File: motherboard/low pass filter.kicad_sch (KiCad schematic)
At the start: 12 parts, among them U4 LM324

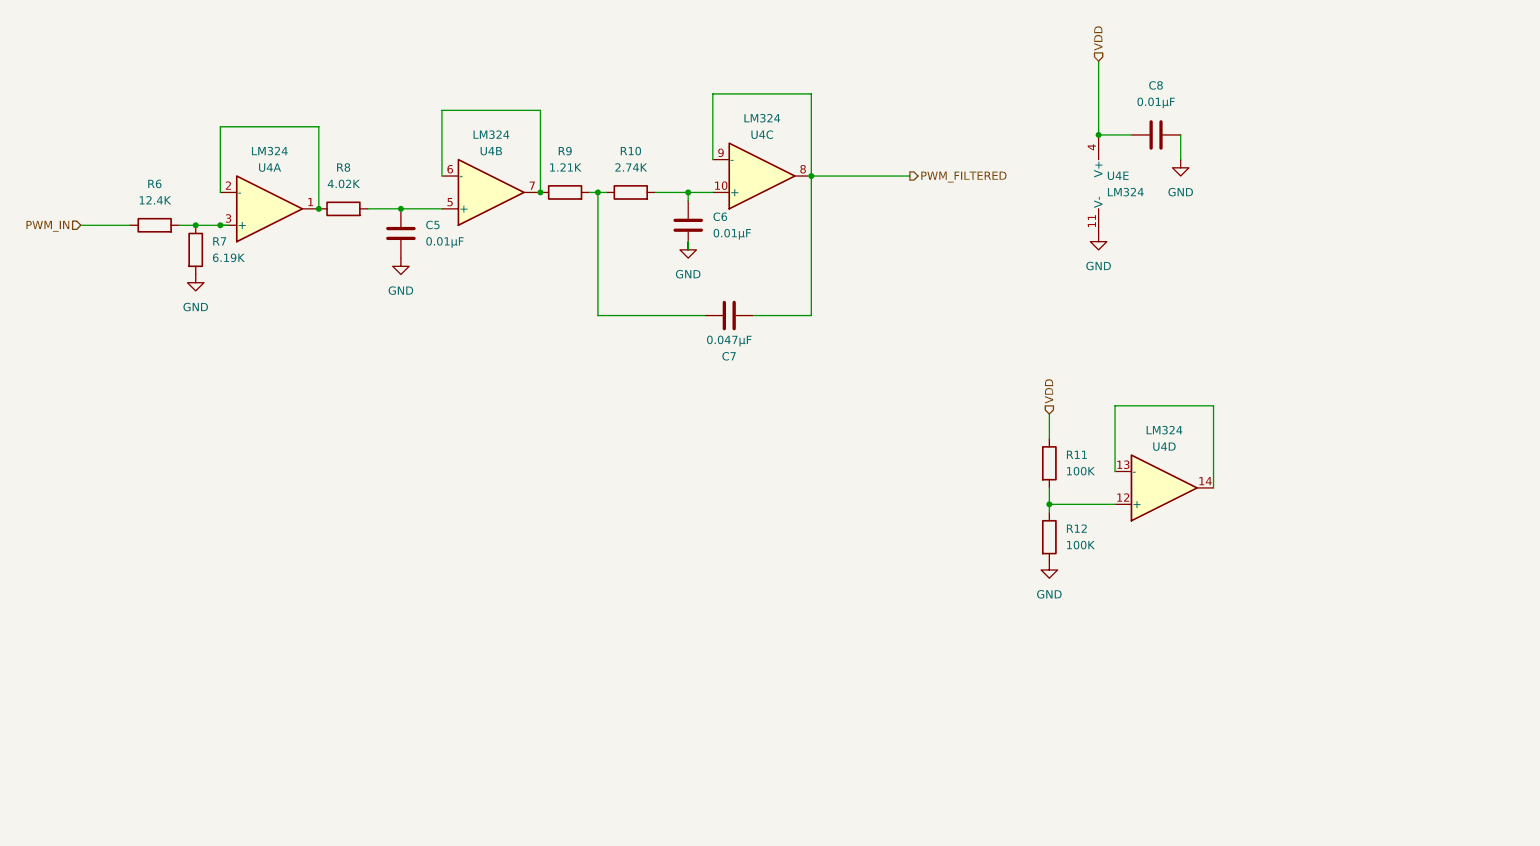
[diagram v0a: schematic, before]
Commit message: motherboard add test points
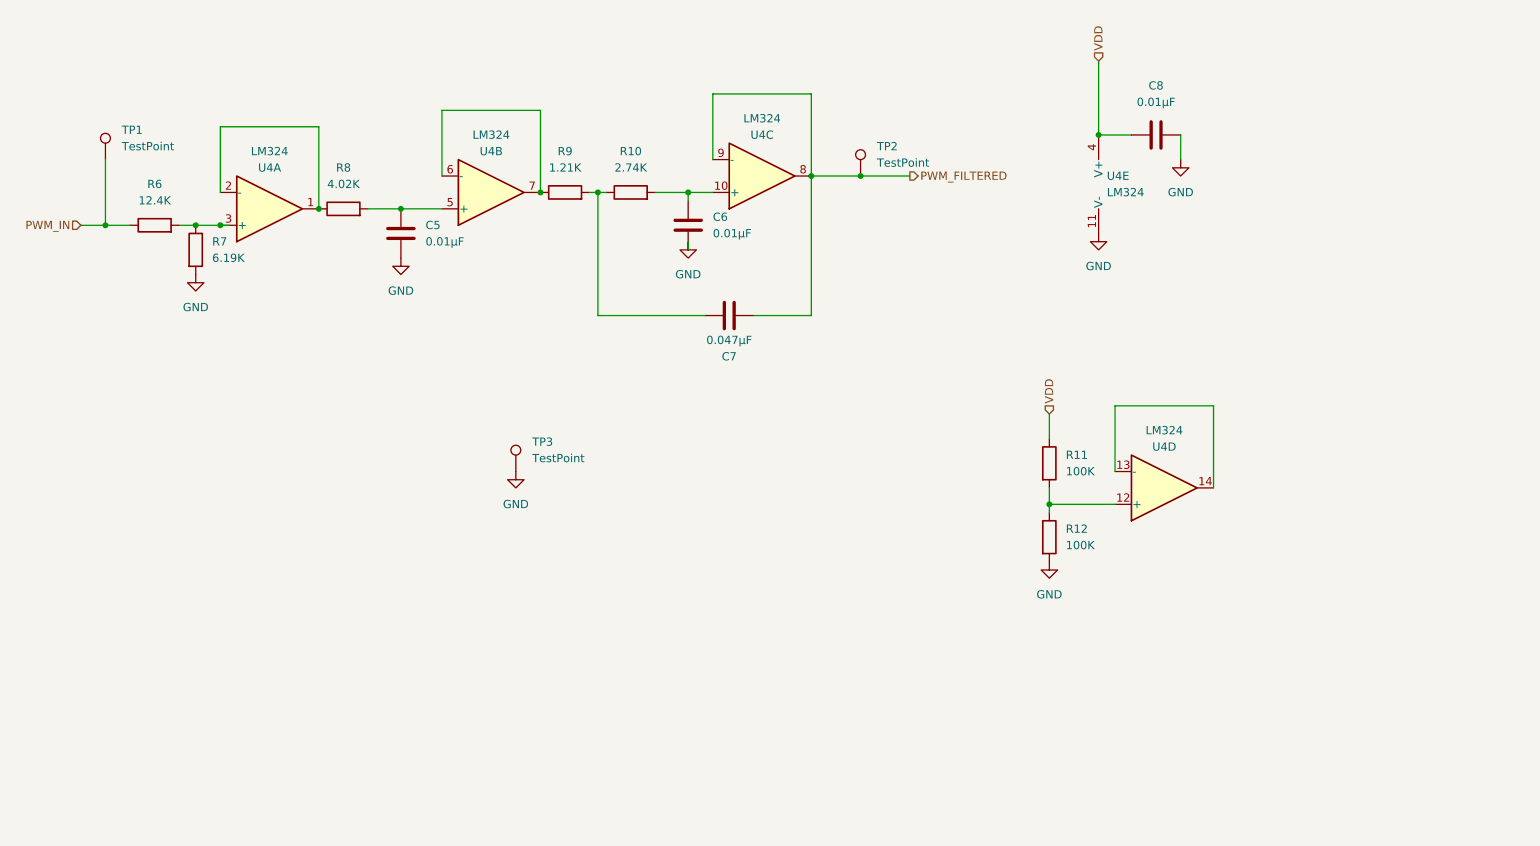
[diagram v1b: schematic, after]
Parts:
- added TP1, TP2: TestPoint, TestPoint:TestPoint_THTPad_D1.0mm_Drill0.5mm, symbol Connector:TestPoint
- added TP3: TestPoint, TestPoint:TestPoint_THTPad_1.0x1.0mm_Drill0.5mm, symbol Connector:TestPoint
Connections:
- net GND: now also TP3.1
- net PWM_FILTERED: now also TP2.1
- net PWM_IN: now also TP1.1
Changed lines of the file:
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@@
   (junction (at 97.79 53.34) (diameter 0) (color 0 0 0 0)
   )
+  (junction (at 147.32 50.8) (diameter 0) (color 0 0 0 0)
+  )
   (junction (at 63.5 55.88) (diameter 0) (color 0 0 0 0)
   )
@@
   (junction (at 76.2 55.88) (diameter 0) (color 0 0 0 0)
   )
+  (junction (at 30.48 58.42) (diameter 0) (color 0 0 0 0)
+  )
   (junction (at 106.68 53.34) (diameter 0) (color 0 0 0 0)
   )
@@
     (stroke (width 0) (type default))
   )
-  (wire (pts (xy 26.67 58.42) (xy 34.29 58.42))
+  (wire (pts (xy 26.67 58.42) (xy 30.48 58.42))
     (stroke (width 0) (type default))
   )
@@
     (stroke (width 0) (type default))
   )
+  (wire (pts (xy 30.48 58.42) (xy 34.29 58.42))
+    (stroke (width 0) (type default))
+  )
   (wire (pts (xy 201.93 86.36) (xy 186.69 86.36))
     (stroke (width 0) (type default))
@@
     (stroke (width 0) (type default))
   )
+  (wire (pts (xy 30.48 48.26) (xy 30.48 58.42))
+    (stroke (width 0) (type default))
+  )
   (wire (pts (xy 48.26 53.34) (xy 48.26 43.18))
     (stroke (width 0) (type default))
@@
     (stroke (width 0) (type default))
   )
+  (wire (pts (xy 147.32 50.8) (xy 154.94 50.8))
+    (stroke (width 0) (type default))
+  )
   (wire (pts (xy 176.53 101.6) (xy 176.53 102.87))
     (stroke (width 0) (type default))
@@
     (stroke (width 0) (type default))
   )
-  (wire (pts (xy 139.7 50.8) (xy 154.94 50.8))
+  (wire (pts (xy 139.7 50.8) (xy 147.32 50.8))
     (stroke (width 0) (type default))
   )
@@
         (path "/e63e39d7-6ac0-4ffd-8aa3-1841a4541b55/ea3171e1-d7f3-4749-80f8-d8022d132810"
           (reference "#PWR027") (unit 1)
+        )
+      )
+    )
+  )
+  (symbol (lib_id "power:GND") (at 93.98 96.52 0) (unit 1)
+    (in_bom yes) (on_board yes) (dnp no) (fields_autoplaced)
+    (property "Reference" "#PWR034" (at 93.98 102.87 0)
+      (effects (font (size 1.27 1.27)) hide)
+    )
+    (property "Value" "GND" (at 93.98 101.6 0)
+      (effects (font (size 1.27 1.27)))
+    )
+    (property "Footprint" "" (at 93.98 96.52 0)
+      (effects (font (size 1.27 1.27)) hide)
+    )
+    (property "Datasheet" "" (at 93.98 96.52 0)
+      (effects (font (size 1.27 1.27)) hide)
+    )
+    (pin "1")
+    (instances
+      (project "motherboard"
+        (path "/e63e39d7-6ac0-4ffd-8aa3-1841a4541b55/ea3171e1-d7f3-4749-80f8-d8022d132810"
+          (reference "#PWR034") (unit 1)
         )
       )
@@
     )
   )
+  (symbol (lib_id "Connector:TestPoint") (at 30.48 48.26 0) (unit 1)
+    (in_bom yes) (on_board yes) (dnp no) (fields_autoplaced)
+    (property "Reference" "TP1" (at 33.02 43.688 0)
+      (effects (font (size 1.27 1.27)) (justify left))
+    )
+    (property "Value" "TestPoint" (at 33.02 46.228 0)
+      (effects (font (size 1.27 1.27)) (justify left))
+    )
+    (property "Footprint" "TestPoint:TestPoint_THTPad_D1.0mm_Drill0.5mm" (at 35.56 48.26 0)
+      (effects (font (size 1.27 1.27)) hide)
+    )
+    (property "Datasheet" "~" (at 35.56 48.26 0)
+      (effects (font (size 1.27 1.27)) hide)
+    )
+    (pin "1")
+    (instances
+      (project "motherboard"
+        (path "/e63e39d7-6ac0-4ffd-8aa3-1841a4541b55/ea3171e1-d7f3-4749-80f8-d8022d132810"
+          (reference "TP1") (unit 1)
+        )
+      )
+    )
+  )
   (symbol (lib_id "Amplifier_Operational:LM324") (at 186.69 52.07 0) (unit 5)
     (in_bom yes) (on_board yes) (dnp no) (fields_autoplaced)
@@
     )
   )
+  (symbol (lib_id "Connector:TestPoint") (at 93.98 96.52 0) (unit 1)
+    (in_bom yes) (on_board yes) (dnp no) (fields_autoplaced)
+    (property "Reference" "TP3" (at 96.52 91.948 0)
+      (effects (font (size 1.27 1.27)) (justify left))
+    )
+    (property "Value" "TestPoint" (at 96.52 94.488 0)
+      (effects (font (size 1.27 1.27)) (justify left))
+    )
+    (property "Footprint" "TestPoint:TestPoint_THTPad_1.0x1.0mm_Drill0.5mm" (at 99.06 96.52 0)
+      (effects (font (size 1.27 1.27)) hide)
+    )
+    (property "Datasheet" "~" (at 99.06 96.52 0)
+      (effects (font (size 1.27 1.27)) hide)
+    )
+    (pin "1")
+    (instances
+      (project "motherboard"
+        (path "/e63e39d7-6ac0-4ffd-8aa3-1841a4541b55/ea3171e1-d7f3-4749-80f8-d8022d132810"
+          (reference "TP3") (unit 1)
+        )
+      )
+    )
+  )
   (symbol (lib_id "Amplifier_Operational:LM324") (at 90.17 53.34 0) (mirror x) (unit 2)
     (in_bom yes) (on_board yes) (dnp no)
@@
         )
       )
+    )
+  )
+  (symbol (lib_id "Connector:TestPoint") (at 147.32 50.8 0) (unit 1)
+    (in_bom yes) (on_board yes) (dnp no) (fields_autoplaced)
+    (property "Reference" "TP2" (at 149.86 46.228 0)
+      (effects (font (size 1.27 1.27)) (justify left))
+    )
+    (property "Value" "TestPoint" (at 149.86 48.768 0)
+      (effects (font (size 1.27 1.27)) (justify left))
+    )
+    (property "Footprint" "TestPoint:TestPoint_THTPad_D1.0mm_Drill0.5mm" (at 152.4 50.8 0)
+      (effects (font (size 1.27 1.27)) hide)
+    )
+    (property "Datasheet" "~" (at 152.4 50.8 0)
+      (effects (font (size 1.27 1.27)) hide)
+    )
+    (pin "1")
+    (instances
+      (project "motherboard"
+        (path "/e63e39d7-6ac0-4ffd-8aa3-1841a4541b55/ea3171e1-d7f3-4749-80f8-d8022d132810"
+          (reference "TP2") (unit 1)
+        )
+      )

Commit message: add 1st order low pass filter, with solder jumper
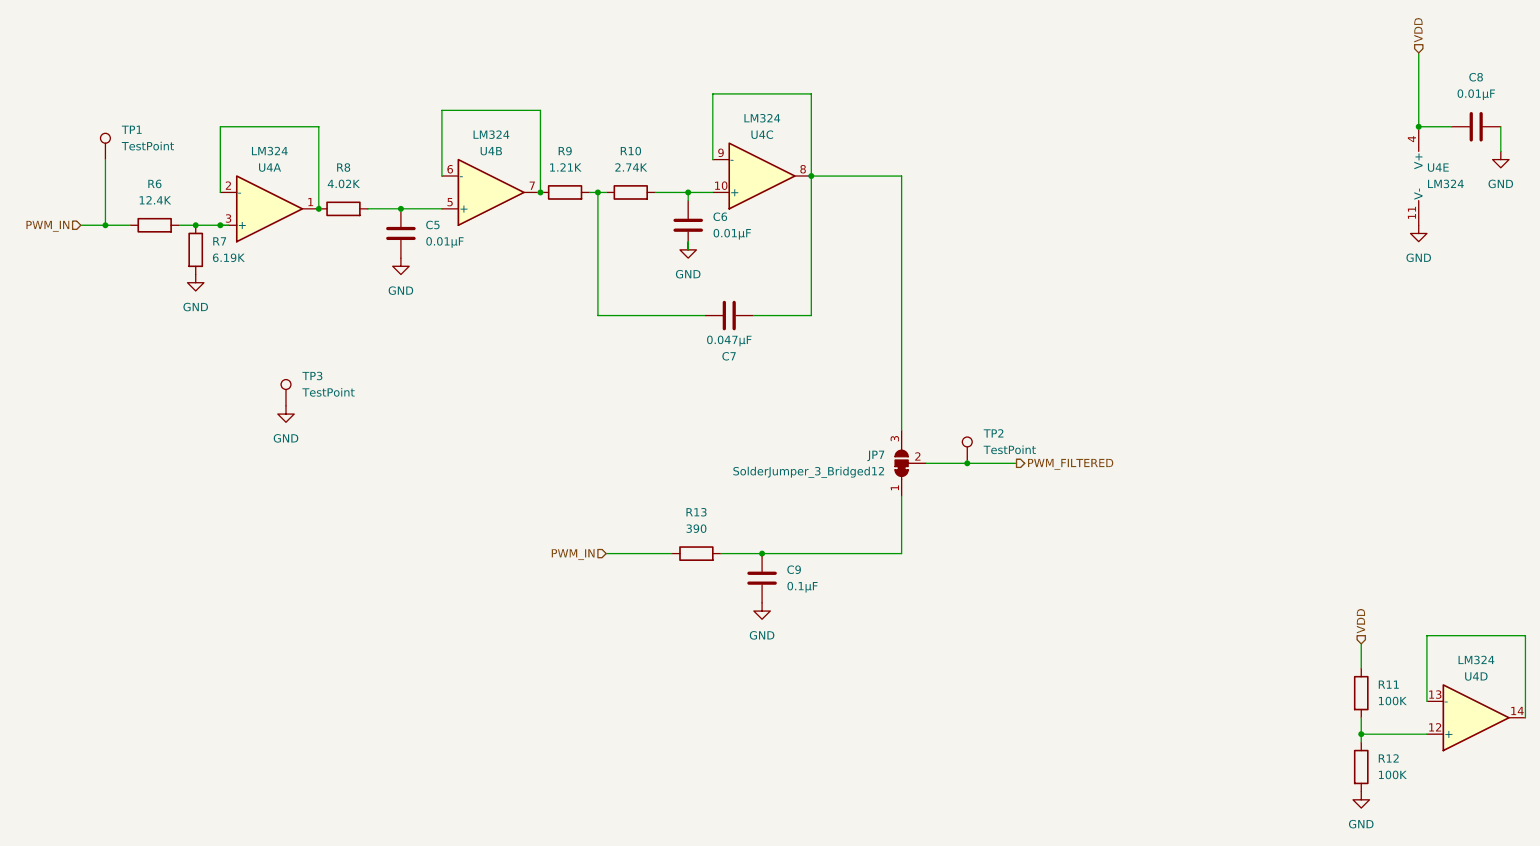
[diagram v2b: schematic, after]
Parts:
- added C9: 0.1µF, Capacitor_SMD:C_0603_1608Metric, symbol Device:C
- added JP7: SolderJumper_3_Bridged12, Jumper:SolderJumper-3_P1.3mm_Bridged12_Pad1.0x1.5mm, symbol Jumper:SolderJumper_3_Bridged12
- added R13: 390, Resistor_SMD:R_0603_1608Metric, symbol Device:R
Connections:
- net GND: now also C9.2
- net PWM_FILTERED: now also JP7.2 (C); no longer C7.2, U4.8, U4.9 (-)
- net PWM_IN: now also R13.1
- new net: C9.1, JP7.1 (A), R13.2
- new net: C7.2, JP7.3 (B), U4.8, U4.9 (-)
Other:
- moved on the sheet: C8, R11, R12, TP2, TP3, U4D, U4E
